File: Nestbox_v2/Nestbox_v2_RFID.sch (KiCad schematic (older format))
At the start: 15 parts, among them U401 MLX90109

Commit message: created V2 MLX breakout board
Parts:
- removed AE401: Antenna_Loop, symbol Antenna_Loop
- removed C401, C402, C403, C404: C, symbol C
- removed R403, R404, R405, R406: R, symbol R
- removed U401: MLX90109, symbol MLX90109
- added J?: CONN_01X05, symbol CONN_01X05
- added R? (x2): 18k, symbol R
- added R? (x2): 33k, symbol R
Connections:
- net labels added: RFID_MODU
- wire segments 34 -> 29
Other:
- note removed: "!! TODO: add pull-ups for clk and data\n"
- note removed: "TODO: add possibility to place up to 3 antenna coils in series"
- moved on the sheet: C405, JP401, Q?, R401, R402

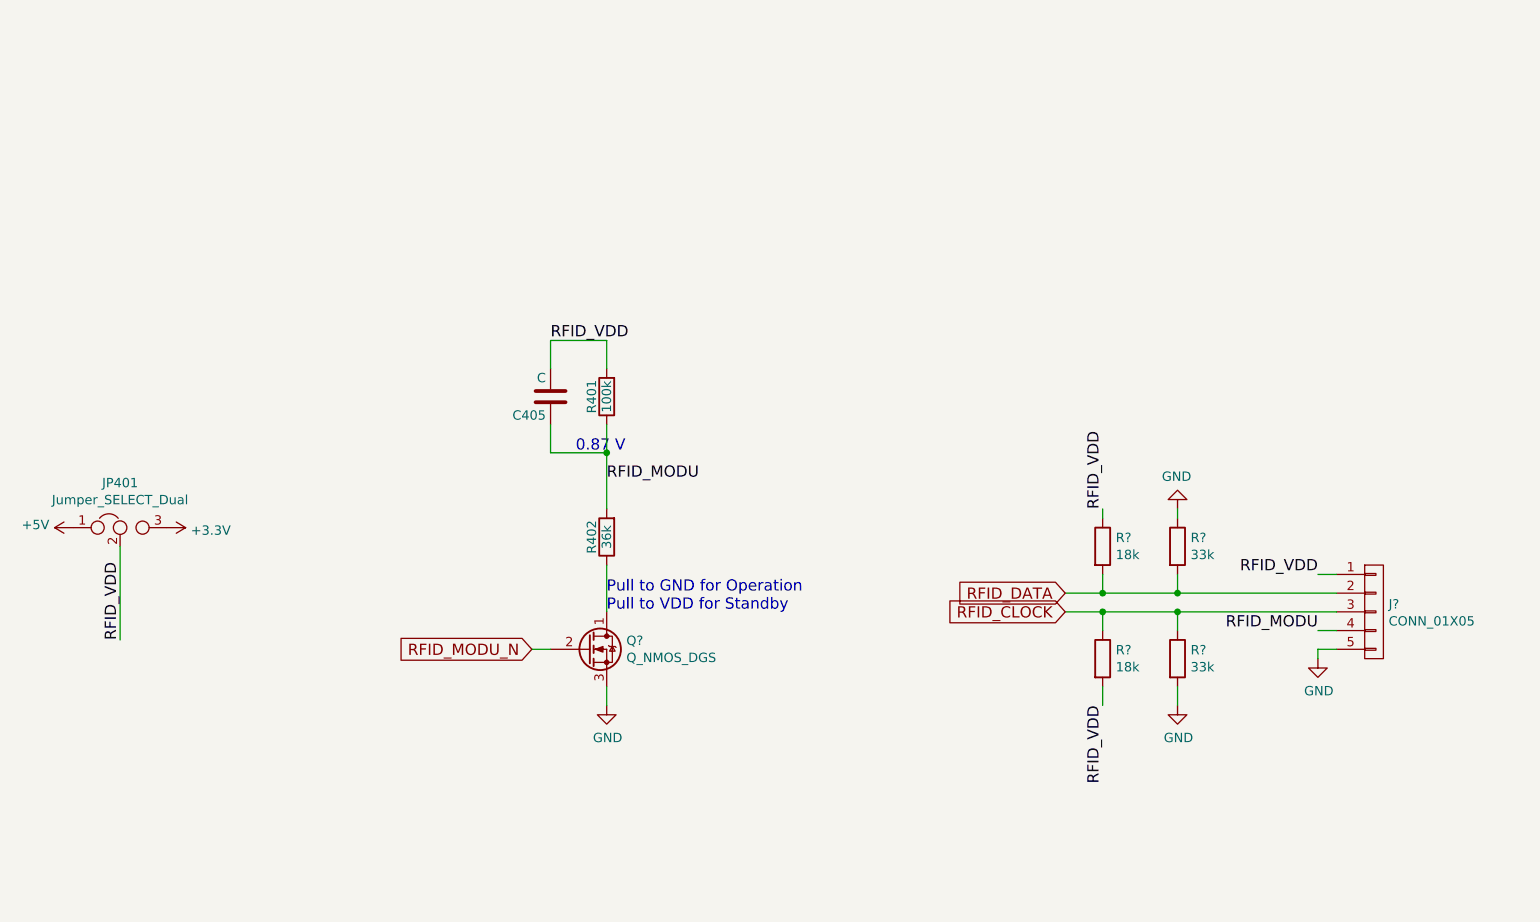
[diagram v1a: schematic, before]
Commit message: restructured top level sheet with hierarchical labels, assigned most GPIOs
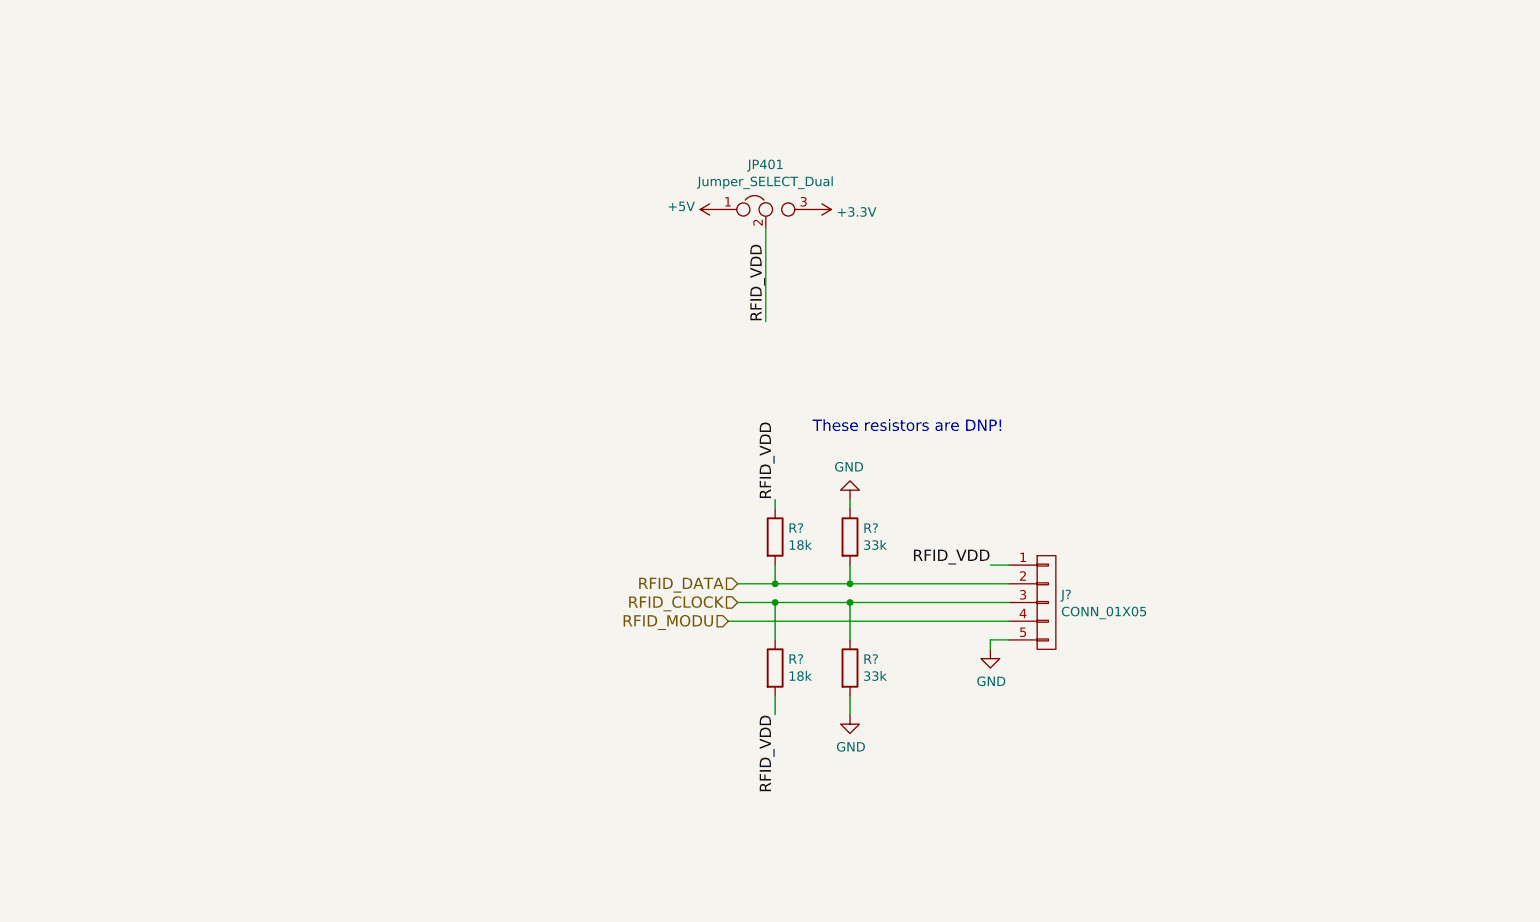
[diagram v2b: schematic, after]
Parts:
- removed C405: C, symbol C
- removed Q?: Q_NMOS_DGS, symbol Q_NMOS_DGS
- removed R401: 100k, symbol R
- removed R402: 36k, symbol R
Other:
- note added: "These resistors are DNP!\n"
- note removed: "0.87 V"
- note removed: "Pull to GND for Operation\nPull to VDD for Standby\n"
- moved on the sheet: J?, JP401, R?

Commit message: finished power supply schematics
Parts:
- removed J?: CONN_01X05, symbol CONN_01X05
- added J?: CONN_01X05, symbol CONN_01X05
- added Q?: Q_NMOS_DGS, symbol Q_NMOS_DGS
- added R?: 50k, symbol R
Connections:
- net GND: now also J?.5 (P5), Q?.3 (S)
- net RFID_CLOCK: now also R?.2, R?.2, J?.2 (P2); no longer R?.1, R?.1
- net RFID_DATA: now also R?.1, R?.1, J?.3 (P3); no longer R?.2, R?.2
- net RFID_VDD: now also J?.1 (P1), R?.2
- net +3V3 renamed +BATT
- new net: J?.4 (P4), Q?.1 (D), R?.1
- new net RFID_SLEEP_N: Q?.2 (G)
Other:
- moved on the sheet: R?
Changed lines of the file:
@@
 Comment4 ""
 $EndDescr
-$Comp
-L +3.3V #PWR048
-U 1 1 59FF36B1
-P 5800 2300
-F 0 "#PWR048" H 5800 2150 50  0001 C CNN
-F 1 "+3.3V" V 5815 2428 50  0000 L CNN
-F 2 "" H 5800 2300 50  0000 C CNN
-F 3 "" H 5800 2300 50  0000 C CNN
-	1    5800 2300
-	0    1    1    0
-$EndComp
 Text Label 6750 4200 2    60   ~ 0
 RFID_VDD
@@
 L +5V #PWR049
 U 1 1 5A0305A8
-P 5300 2300
-F 0 "#PWR049" H 5300 2150 50  0001 C CNN
-F 1 "+5V" V 5315 2428 50  0000 L CNN
-F 2 "" H 5300 2300 50  0001 C CNN
-F 3 "" H 5300 2300 50  0001 C CNN
-	1    5300 2300
+P 5200 2300
+F 0 "#PWR049" H 5200 2150 50  0001 C CNN
+F 1 "+5V" V 5215 2428 50  0000 L CNN
+F 2 "" H 5200 2300 50  0001 C CNN
+F 3 "" H 5200 2300 50  0001 C CNN
+	1    5200 2300
 	0    -1   -1   0
 $EndComp
@@
 L R R?
 U 1 1 5AF8A741
-P 5600 4750
-F 0 "R?" H 5670 4796 50  0000 L CNN
-F 1 "18k" H 5670 4705 50  0000 L CNN
-F 2 "" V 5530 4750 50  0001 C CNN
-F 3 "" H 5600 4750 50  0001 C CNN
-	1    5600 4750
+P 5600 4850
+F 0 "R?" H 5670 4896 50  0000 L CNN
+F 1 "18k" H 5670 4805 50  0000 L CNN
+F 2 "" V 5530 4850 50  0001 C CNN
+F 3 "" H 5600 4850 50  0001 C CNN
+	1    5600 4850
 	1    0    0    -1
 $EndComp
@@
 L R R?
 U 1 1 5AF8AB4E
-P 6000 4750
-F 0 "R?" H 6070 4796 50  0000 L CNN
-F 1 "33k" H 6070 4705 50  0000 L CNN
-F 2 "" V 5930 4750 50  0001 C CNN
-F 3 "" H 6000 4750 50  0001 C CNN
-	1    6000 4750
+P 6000 4850
+F 0 "R?" H 6070 4896 50  0000 L CNN
+F 1 "33k" H 6070 4805 50  0000 L CNN
+F 2 "" V 5930 4850 50  0001 C CNN
+F 3 "" H 6000 4850 50  0001 C CNN
+	1    6000 4850
 	1    0    0    -1
 $EndComp
@@
 L GND #PWR?
 U 1 1 5AF8AC8E
-P 6000 5000
-F 0 "#PWR?" H 6000 4750 50  0001 C CNN
-F 1 "GND" H 6005 4827 50  0000 C CNN
-F 2 "" H 6000 5000 50  0001 C CNN
-F 3 "" H 6000 5000 50  0001 C CNN
-	1    6000 5000
-	1    0    0    -1
-$EndComp
-Wire Wire Line
-	6000 4900 6000 5000
+P 6000 5100
+F 0 "#PWR?" H 6000 4850 50  0001 C CNN
+F 1 "GND" H 6005 4927 50  0000 C CNN
+F 2 "" H 6000 5100 50  0001 C CNN
+F 3 "" H 6000 5100 50  0001 C CNN
+	1    6000 5100
+	1    0    0    -1
+$EndComp
+Wire Wire Line
+	6000 5000 6000 5100
 Wire Wire Line
 	6000 3900 6000 3850
 Connection ~ 6000 4400
 Wire Wire Line
-	6000 4400 6000 4600
+	6000 4400 6000 4700
 Connection ~ 6000 4300
 Wire Wire Line
 	6000 4300 6000 4200
 Wire Wire Line
-	5600 4900 5600 5000
+	5600 5000 5600 5100
 Wire Wire Line
 	5600 3850 5600 3900
@@
 Connection ~ 5600 4400
 Wire Wire Line
-	5600 4400 5600 4600
-Wire Wire Line
-	5350 4500 6850 4500
+	5600 4400 5600 4700
 Wire Wire Line
 	5400 4400 6850 4400
@@
 Text Label 5600 3850 1    60   ~ 0
 RFID_VDD
-Text Label 5600 5000 3    60   ~ 0
-RFID_VDD
+Text Label 5600 5100 3    60   ~ 0
+RFID_VDD
+$Comp
+L GND #PWR?
+U 1 1 5AF8B903
+P 6750 4750
+F 0 "#PWR?" H 6750 4500 50  0001 C CNN
+F 1 "GND" H 6755 4577 50  0000 C CNN
+F 2 "" H 6750 4750 50  0001 C CNN
+F 3 "" H 6750 4750 50  0001 C CNN
+	1    6750 4750
+	1    0    0    -1
+$EndComp
+Text HLabel 5400 4400 0    60   Input ~ 0
+RFID_DATA
+Text HLabel 5400 4300 0    60   Input ~ 0
+RFID_CLOCK
+Text Notes 5800 3500 0    60   ~ 0
+These resistors are DNP!\n
+$Comp
+L Q_NMOS_DGS Q?
+U 1 1 5B08713B
+P 4250 4800
+F 0 "Q?" H 4450 4850 50  0000 L CNN
+F 1 "Q_NMOS_DGS" H 4450 4750 50  0000 L CNN
+F 2 "" H 4450 4900 50  0001 C CNN
+F 3 "" H 4250 4800 50  0001 C CNN
+	1    4250 4800
+	1    0    0    -1
+$EndComp
+Text Label 5150 5100 3    60   ~ 0
+RFID_VDD
+Wire Wire Line
+	5150 5100 5150 5000
+$Comp
+L GND #PWR?
+U 1 1 5B088780
+P 4350 5000
+F 0 "#PWR?" H 4350 4750 50  0001 C CNN
+F 1 "GND" H 4355 4827 50  0000 C CNN
+F 2 "" H 4350 5000 50  0001 C CNN
+F 3 "" H 4350 5000 50  0001 C CNN
+	1    4350 5000
+	1    0    0    -1
+$EndComp
+Text HLabel 4000 4800 0    60   Input ~ 0
+RFID_SLEEP_N
+Wire Wire Line
+	4000 4800 4050 4800
+Wire Wire Line
+	4350 4600 4350 4500
+Wire Wire Line
+	4350 4500 6850 4500
+$Comp
+L R R?
+U 1 1 5B088617
+P 5150 4850
+F 0 "R?" H 5220 4896 50  0000 L CNN
+F 1 "50k" H 5220 4805 50  0000 L CNN
+F 2 "" V 5080 4850 50  0001 C CNN
+F 3 "" H 5150 4850 50  0001 C CNN
+	1    5150 4850
+	1    0    0    -1
+$EndComp
+Wire Wire Line
+	5150 4700 5150 4500
+Connection ~ 5150 4500
+Wire Wire Line
+	6750 4600 6850 4600
 $Comp
 L CONN_01X05 J?
-U 1 1 5AF8B87E
+U 1 1 5B08A8CB
 P 7050 4400
-F 0 "J?" H 7128 4441 50  0000 L CNN
-F 1 "CONN_01X05" H 7128 4350 50  0000 L CNN
+F 0 "J?" H 7050 4700 50  0000 C CNN
+F 1 "CONN_01X05" V 7150 4400 50  0000 C CNN
 F 2 "" H 7050 4400 50  0001 C CNN
 F 3 "" H 7050 4400 50  0001 C CNN
@@
 	1    0    0    -1
 $EndComp
-$Comp
-L GND #PWR?
-U 1 1 5AF8B903
-P 6750 4650
-F 0 "#PWR?" H 6750 4400 50  0001 C CNN
-F 1 "GND" H 6755 4477 50  0000 C CNN
-F 2 "" H 6750 4650 50  0001 C CNN
-F 3 "" H 6750 4650 50  0001 C CNN
-	1    6750 4650
-	1    0    0    -1
-$EndComp
-Wire Wire Line
-	6850 4600 6750 4600
-Wire Wire Line
-	6750 4600 6750 4650
-Text HLabel 5400 4300 0    60   Input ~ 0
-RFID_DATA
-Text HLabel 5400 4400 0    60   Input ~ 0
-RFID_CLOCK
-Text HLabel 5350 4500 0    60   Input ~ 0
-RFID_MODU
-Text Notes 5800 3500 0    60   ~ 0
-These resistors are DNP!\n
+Wire Wire Line
+	6750 4750 6750 4600
+Wire Wire Line
+	5800 2300 5950 2300
+Wire Wire Line
+	5200 2300 5300 2300
+$Comp
+L +BATT #PWR?
+U 1 1 5B08AE2C
+P 5950 2300
+F 0 "#PWR?" H 5950 2150 50  0001 C CNN
+F 1 "+BATT" H 5950 2440 50  0000 C CNN
+F 2 "" H 5950 2300 50  0001 C CNN
+F 3 "" H 5950 2300 50  0001 C CNN
+	1    5950 2300
+	0    1    1    0
+$EndComp
 $EndSCHEMATC

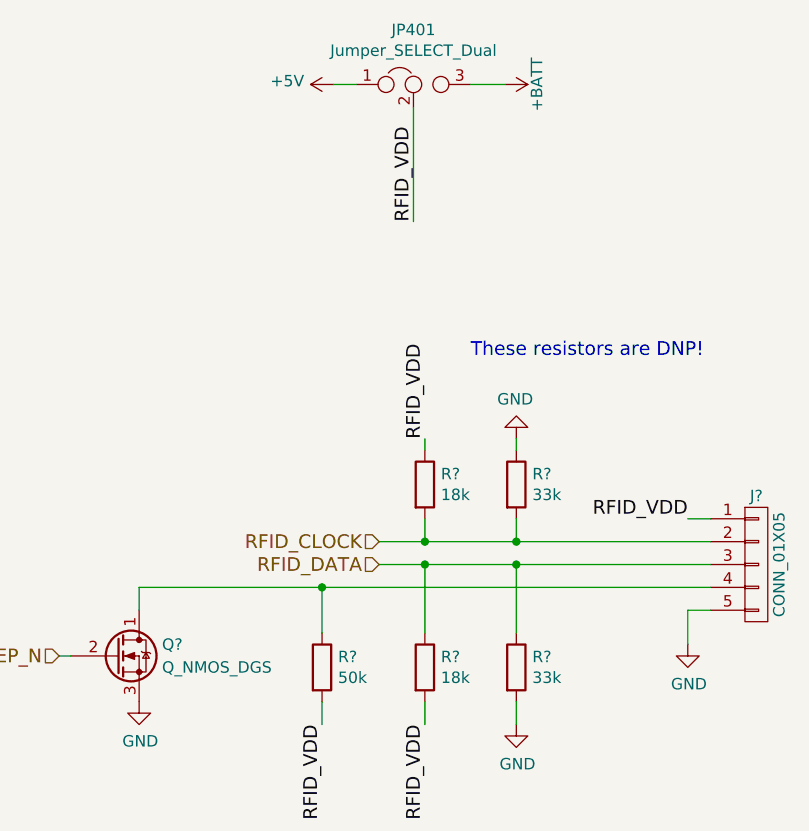
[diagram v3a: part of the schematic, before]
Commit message: added PIR and lightbarrier headers
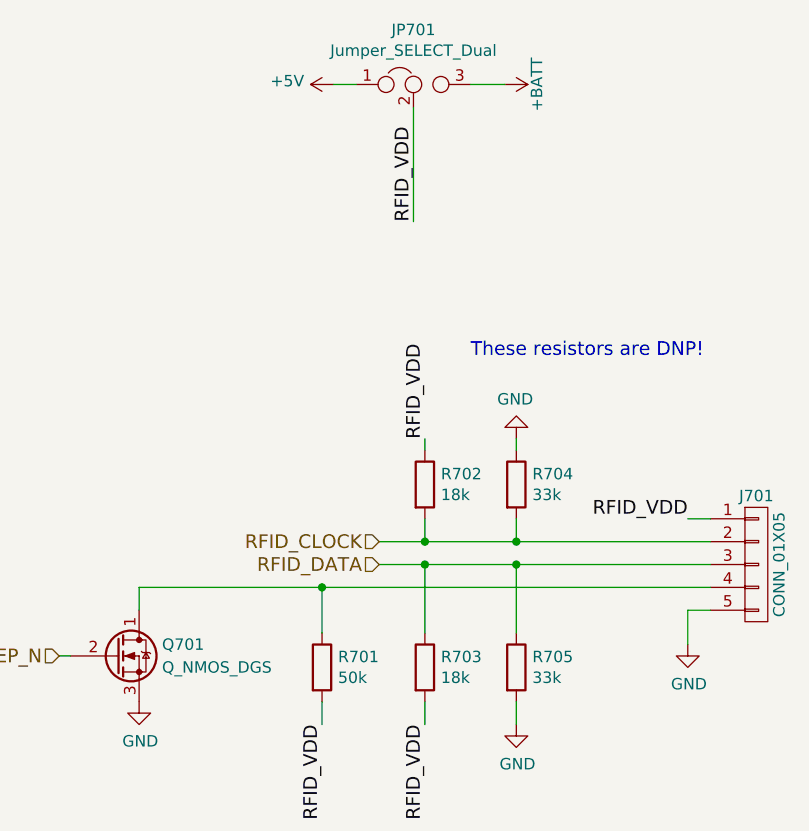
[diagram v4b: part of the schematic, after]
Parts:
- gave numbers to parts that had none: 7
- renumbered JP401 to JP701
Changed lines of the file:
@@
 $Descr A4 11693 8268
 encoding utf-8
-Sheet 4 7
+Sheet 7 7
 Title ""
 Date ""
@@
 RFID_VDD
 $Comp
-L Jumper_SELECT_Dual JP401
+L Jumper_SELECT_Dual JP701
 U 1 1 5A0303B0
 P 5550 2300
-F 0 "JP401" H 5550 2539 50  0000 C CNN
+F 0 "JP701" H 5550 2539 50  0000 C CNN
 F 1 "Jumper_SELECT_Dual" H 5550 2448 50  0000 C CNN
 F 2 "" H 5550 2300 50  0001 C CNN
@@
 RFID_VDD
 $Comp
-L +5V #PWR049
+L +5V #PWR084
 U 1 1 5A0305A8
 P 5200 2300
-F 0 "#PWR049" H 5200 2150 50  0001 C CNN
+F 0 "#PWR084" H 5200 2150 50  0001 C CNN
 F 1 "+5V" V 5215 2428 50  0000 L CNN
 F 2 "" H 5200 2300 50  0001 C CNN
@@
 $EndComp
 $Comp
-L R R?
+L R R702
 U 1 1 5AF8A68B
 P 5600 4050
-F 0 "R?" H 5670 4096 50  0000 L CNN
+F 0 "R702" H 5670 4096 50  0000 L CNN
 F 1 "18k" H 5670 4005 50  0000 L CNN
 F 2 "" V 5530 4050 50  0001 C CNN
@@
 $EndComp
 $Comp
-L R R?
+L R R703
 U 1 1 5AF8A741
 P 5600 4850
-F 0 "R?" H 5670 4896 50  0000 L CNN
+F 0 "R703" H 5670 4896 50  0000 L CNN
 F 1 "18k" H 5670 4805 50  0000 L CNN
 F 2 "" V 5530 4850 50  0001 C CNN
@@
 $EndComp
 $Comp
-L R R?
+L R R704
 U 1 1 5AF8AAF5
 P 6000 4050
-F 0 "R?" H 6070 4096 50  0000 L CNN
+F 0 "R704" H 6070 4096 50  0000 L CNN
 F 1 "33k" H 6070 4005 50  0000 L CNN
 F 2 "" V 5930 4050 50  0001 C CNN
@@
 $EndComp
 $Comp
-L R R?
+L R R705
 U 1 1 5AF8AB4E
 P 6000 4850
-F 0 "R?" H 6070 4896 50  0000 L CNN
+F 0 "R705" H 6070 4896 50  0000 L CNN
 F 1 "33k" H 6070 4805 50  0000 L CNN
 F 2 "" V 5930 4850 50  0001 C CNN
@@
 $EndComp
 $Comp
-L GND #PWR?
+L GND #PWR085
 U 1 1 5AF8ABAA
 P 6000 3850
-F 0 "#PWR?" H 6000 3600 50  0001 C CNN
+F 0 "#PWR085" H 6000 3600 50  0001 C CNN
 F 1 "GND" H 6005 3677 50  0000 C CNN
 F 2 "" H 6000 3850 50  0001 C CNN
@@
 $EndComp
 $Comp
-L GND #PWR?
+L GND #PWR086
 U 1 1 5AF8AC8E
 P 6000 5100
-F 0 "#PWR?" H 6000 4850 50  0001 C CNN
+F 0 "#PWR086" H 6000 4850 50  0001 C CNN
 F 1 "GND" H 6005 4927 50  0000 C CNN
 F 2 "" H 6000 5100 50  0001 C CNN
@@
 RFID_VDD
 $Comp
-L GND #PWR?
+L GND #PWR087
 U 1 1 5AF8B903
 P 6750 4750
-F 0 "#PWR?" H 6750 4500 50  0001 C CNN
+F 0 "#PWR087" H 6750 4500 50  0001 C CNN
 F 1 "GND" H 6755 4577 50  0000 C CNN
 F 2 "" H 6750 4750 50  0001 C CNN
@@
 These resistors are DNP!\n
 $Comp
-L Q_NMOS_DGS Q?
+L Q_NMOS_DGS Q701
 U 1 1 5B08713B
 P 4250 4800
-F 0 "Q?" H 4450 4850 50  0000 L CNN
+F 0 "Q701" H 4450 4850 50  0000 L CNN
 F 1 "Q_NMOS_DGS" H 4450 4750 50  0000 L CNN
 F 2 "" H 4450 4900 50  0001 C CNN
@@
 	5150 5100 5150 5000
 $Comp
-L GND #PWR?
+L GND #PWR088
 U 1 1 5B088780
 P 4350 5000
-F 0 "#PWR?" H 4350 4750 50  0001 C CNN
+F 0 "#PWR088" H 4350 4750 50  0001 C CNN
 F 1 "GND" H 4355 4827 50  0000 C CNN
 F 2 "" H 4350 5000 50  0001 C CNN
@@
 	4350 4500 6850 4500
 $Comp
-L R R?
+L R R701
 U 1 1 5B088617
 P 5150 4850
-F 0 "R?" H 5220 4896 50  0000 L CNN
+F 0 "R701" H 5220 4896 50  0000 L CNN
 F 1 "50k" H 5220 4805 50  0000 L CNN
 F 2 "" V 5080 4850 50  0001 C CNN
@@
 	6750 4600 6850 4600
 $Comp
-L CONN_01X05 J?
+L CONN_01X05 J701
 U 1 1 5B08A8CB
 P 7050 4400
-F 0 "J?" H 7050 4700 50  0000 C CNN
+F 0 "J701" H 7050 4700 50  0000 C CNN
 F 1 "CONN_01X05" V 7150 4400 50  0000 C CNN
 F 2 "" H 7050 4400 50  0001 C CNN
@@
 	5200 2300 5300 2300
 $Comp
-L +BATT #PWR?
+L +BATT #PWR089
 U 1 1 5B08AE2C
 P 5950 2300
-F 0 "#PWR?" H 5950 2150 50  0001 C CNN
+F 0 "#PWR089" H 5950 2150 50  0001 C CNN
 F 1 "+BATT" H 5950 2440 50  0000 C CNN
 F 2 "" H 5950 2300 50  0001 C CNN

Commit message: added power footprints, final connector footprints
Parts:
- J701: footprint (none) -> Terminal_Blocks:TerminalBlock_Pheonix_PT-3.5mm_5pol
- JP701: footprint (none) -> Pin_Headers:Pin_Header_Straight_1x03_Pitch2.54mm
- Q701: footprint (none) -> TO_SOT_Packages_SMD:SOT-23
- R701, R702, R703, R704, R705: footprint (none) -> Resistors_SMD:R_0603
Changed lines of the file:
@@
 F 0 "JP701" H 5550 2539 50  0000 C CNN
 F 1 "Jumper_SELECT_Dual" H 5550 2448 50  0000 C CNN
-F 2 "" H 5550 2300 50  0001 C CNN
+F 2 "Pin_Headers:Pin_Header_Straight_1x03_Pitch2.54mm" H 5550 2300 50  0001 C CNN
 F 3 "" H 5550 2300 50  0001 C CNN
 	1    5550 2300
@@
 RFID_VDD
 $Comp
-L +5V #PWR084
+L +5V #PWR085
 U 1 1 5A0305A8
 P 5200 2300
-F 0 "#PWR084" H 5200 2150 50  0001 C CNN
+F 0 "#PWR085" H 5200 2150 50  0001 C CNN
 F 1 "+5V" V 5215 2428 50  0000 L CNN
 F 2 "" H 5200 2300 50  0001 C CNN
@@
 F 0 "R702" H 5670 4096 50  0000 L CNN
 F 1 "18k" H 5670 4005 50  0000 L CNN
-F 2 "" V 5530 4050 50  0001 C CNN
+F 2 "Resistors_SMD:R_0603" V 5530 4050 50  0001 C CNN
 F 3 "" H 5600 4050 50  0001 C CNN
 	1    5600 4050
@@
 F 0 "R703" H 5670 4896 50  0000 L CNN
 F 1 "18k" H 5670 4805 50  0000 L CNN
-F 2 "" V 5530 4850 50  0001 C CNN
+F 2 "Resistors_SMD:R_0603" V 5530 4850 50  0001 C CNN
 F 3 "" H 5600 4850 50  0001 C CNN
 	1    5600 4850
@@
 F 0 "R704" H 6070 4096 50  0000 L CNN
 F 1 "33k" H 6070 4005 50  0000 L CNN
-F 2 "" V 5930 4050 50  0001 C CNN
+F 2 "Resistors_SMD:R_0603" V 5930 4050 50  0001 C CNN
 F 3 "" H 6000 4050 50  0001 C CNN
 	1    6000 4050
@@
 F 0 "R705" H 6070 4896 50  0000 L CNN
 F 1 "33k" H 6070 4805 50  0000 L CNN
-F 2 "" V 5930 4850 50  0001 C CNN
+F 2 "Resistors_SMD:R_0603" V 5930 4850 50  0001 C CNN
 F 3 "" H 6000 4850 50  0001 C CNN
 	1    6000 4850
@@
 $EndComp
 $Comp
-L GND #PWR085
+L GND #PWR086
 U 1 1 5AF8ABAA
 P 6000 3850
-F 0 "#PWR085" H 6000 3600 50  0001 C CNN
+F 0 "#PWR086" H 6000 3600 50  0001 C CNN
 F 1 "GND" H 6005 3677 50  0000 C CNN
 F 2 "" H 6000 3850 50  0001 C CNN
@@
 $EndComp
 $Comp
-L GND #PWR086
+L GND #PWR087
 U 1 1 5AF8AC8E
 P 6000 5100
-F 0 "#PWR086" H 6000 4850 50  0001 C CNN
+F 0 "#PWR087" H 6000 4850 50  0001 C CNN
 F 1 "GND" H 6005 4927 50  0000 C CNN
 F 2 "" H 6000 5100 50  0001 C CNN
@@
 RFID_VDD
 $Comp
-L GND #PWR087
+L GND #PWR088
 U 1 1 5AF8B903
 P 6750 4750
-F 0 "#PWR087" H 6750 4500 50  0001 C CNN
+F 0 "#PWR088" H 6750 4500 50  0001 C CNN
 F 1 "GND" H 6755 4577 50  0000 C CNN
 F 2 "" H 6750 4750 50  0001 C CNN
@@
 F 0 "Q701" H 4450 4850 50  0000 L CNN
 F 1 "Q_NMOS_DGS" H 4450 4750 50  0000 L CNN
-F 2 "" H 4450 4900 50  0001 C CNN
+F 2 "TO_SOT_Packages_SMD:SOT-23" H 4450 4900 50  0001 C CNN
 F 3 "" H 4250 4800 50  0001 C CNN
 	1    4250 4800
@@
 	5150 5100 5150 5000
 $Comp
-L GND #PWR088
+L GND #PWR089
 U 1 1 5B088780
 P 4350 5000
-F 0 "#PWR088" H 4350 4750 50  0001 C CNN
+F 0 "#PWR089" H 4350 4750 50  0001 C CNN
 F 1 "GND" H 4355 4827 50  0000 C CNN
 F 2 "" H 4350 5000 50  0001 C CNN
@@
 F 0 "R701" H 5220 4896 50  0000 L CNN
 F 1 "50k" H 5220 4805 50  0000 L CNN
-F 2 "" V 5080 4850 50  0001 C CNN
+F 2 "Resistors_SMD:R_0603" V 5080 4850 50  0001 C CNN
 F 3 "" H 5150 4850 50  0001 C CNN
 	1    5150 4850
@@
 F 0 "J701" H 7050 4700 50  0000 C CNN
 F 1 "CONN_01X05" V 7150 4400 50  0000 C CNN
-F 2 "" H 7050 4400 50  0001 C CNN
+F 2 "Terminal_Blocks:TerminalBlock_Pheonix_PT-3.5mm_5pol" H 7050 4400 50  0001 C CNN
 F 3 "" H 7050 4400 50  0001 C CNN
 	1    7050 4400
@@
 	5200 2300 5300 2300
 $Comp
-L +BATT #PWR089
+L +BATT #PWR090
 U 1 1 5B08AE2C
 P 5950 2300
-F 0 "#PWR089" H 5950 2150 50  0001 C CNN
+F 0 "#PWR090" H 5950 2150 50  0001 C CNN
 F 1 "+BATT" H 5950 2440 50  0000 C CNN
 F 2 "" H 5950 2300 50  0001 C CNN
